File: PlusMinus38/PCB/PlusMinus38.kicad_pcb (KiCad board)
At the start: 2 copper layers, 98.2 x 84.1 mm, 73 parts

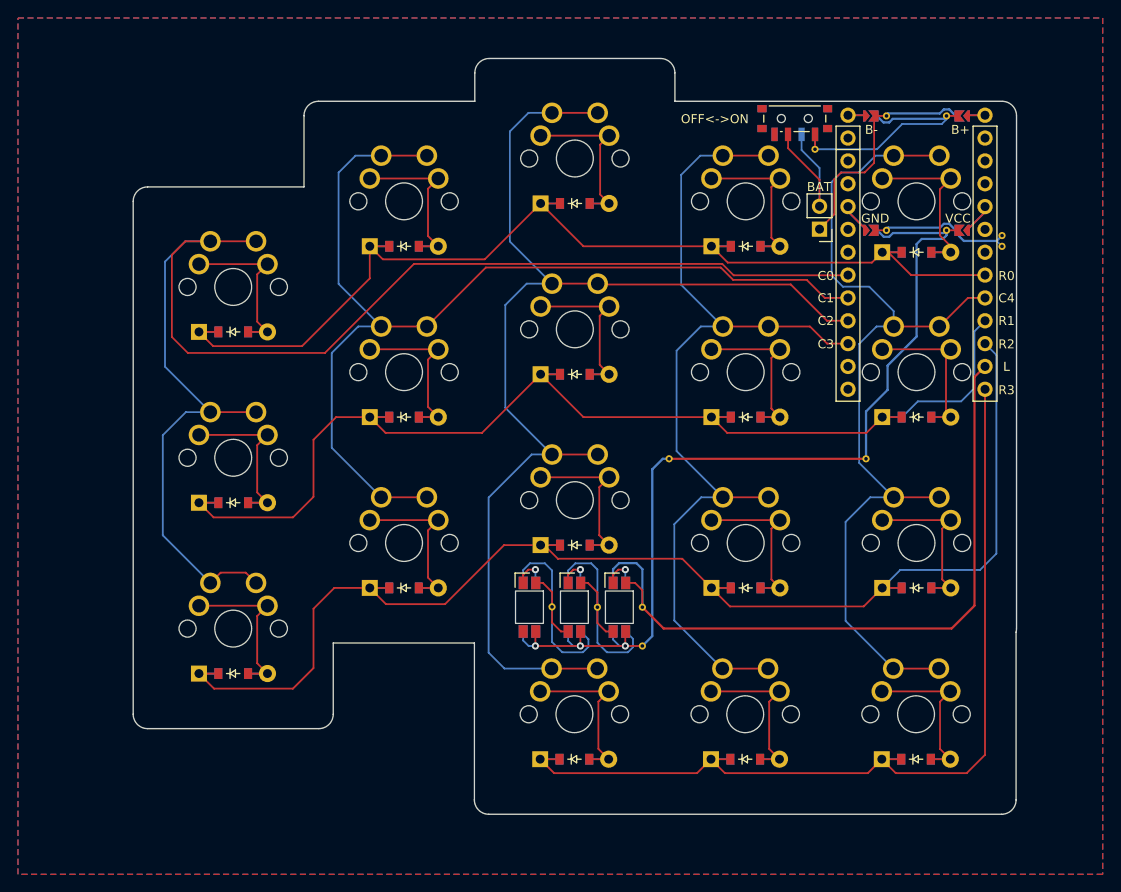
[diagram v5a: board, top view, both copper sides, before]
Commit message: Fixed power line trace width
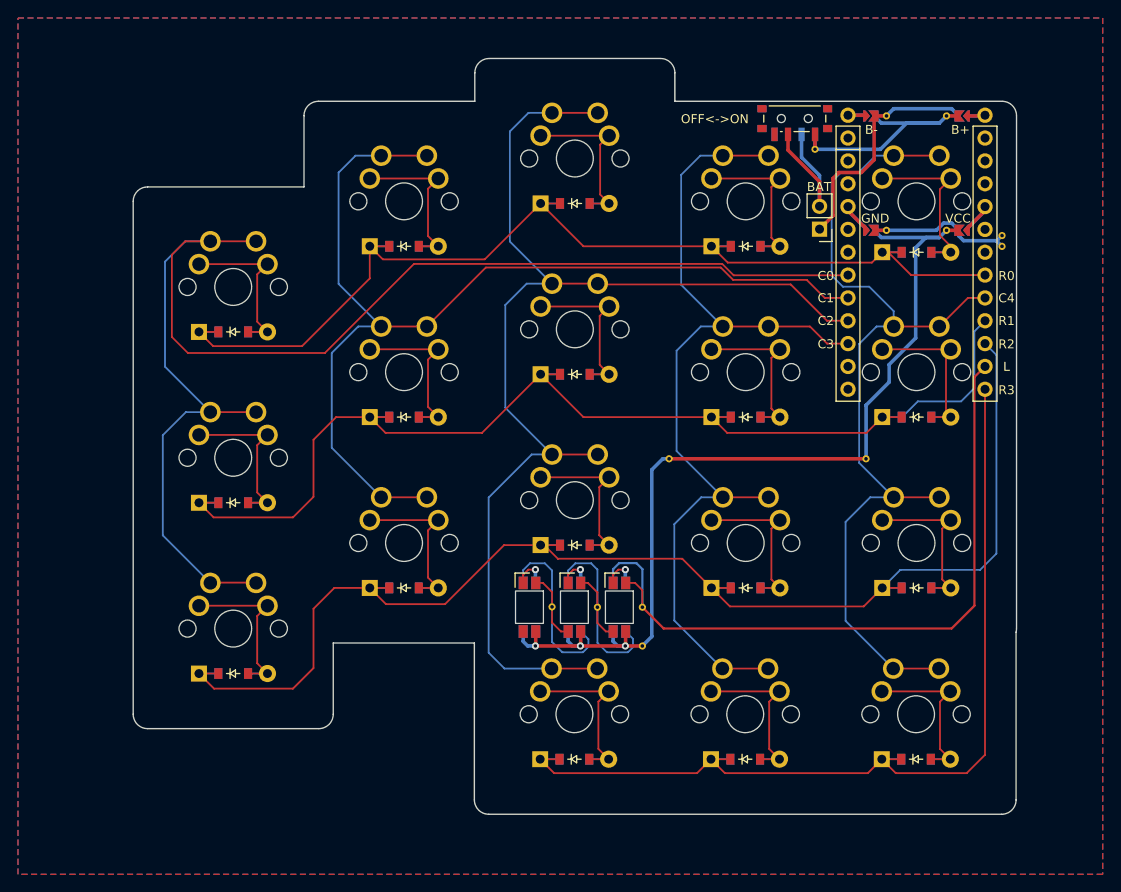
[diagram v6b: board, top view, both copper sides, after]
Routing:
- net VCC: track 109.5 -> 108.3 mm
- net B+: track 29.6 -> 28.5 mm
- net C0: track 160.6 -> 159.7 mm
